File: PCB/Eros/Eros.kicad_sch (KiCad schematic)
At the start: 89 parts, among them J1 USB_C_PowerOnly_6P, J2 UART, J3 Li-ion, J4 Conn_01x08_Socket, J6 Micro_SD_Card, Q1 BC817, SW1 SW_Push, SW2 SW_Push, SW3 SW_Push, SW4 SW_Push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

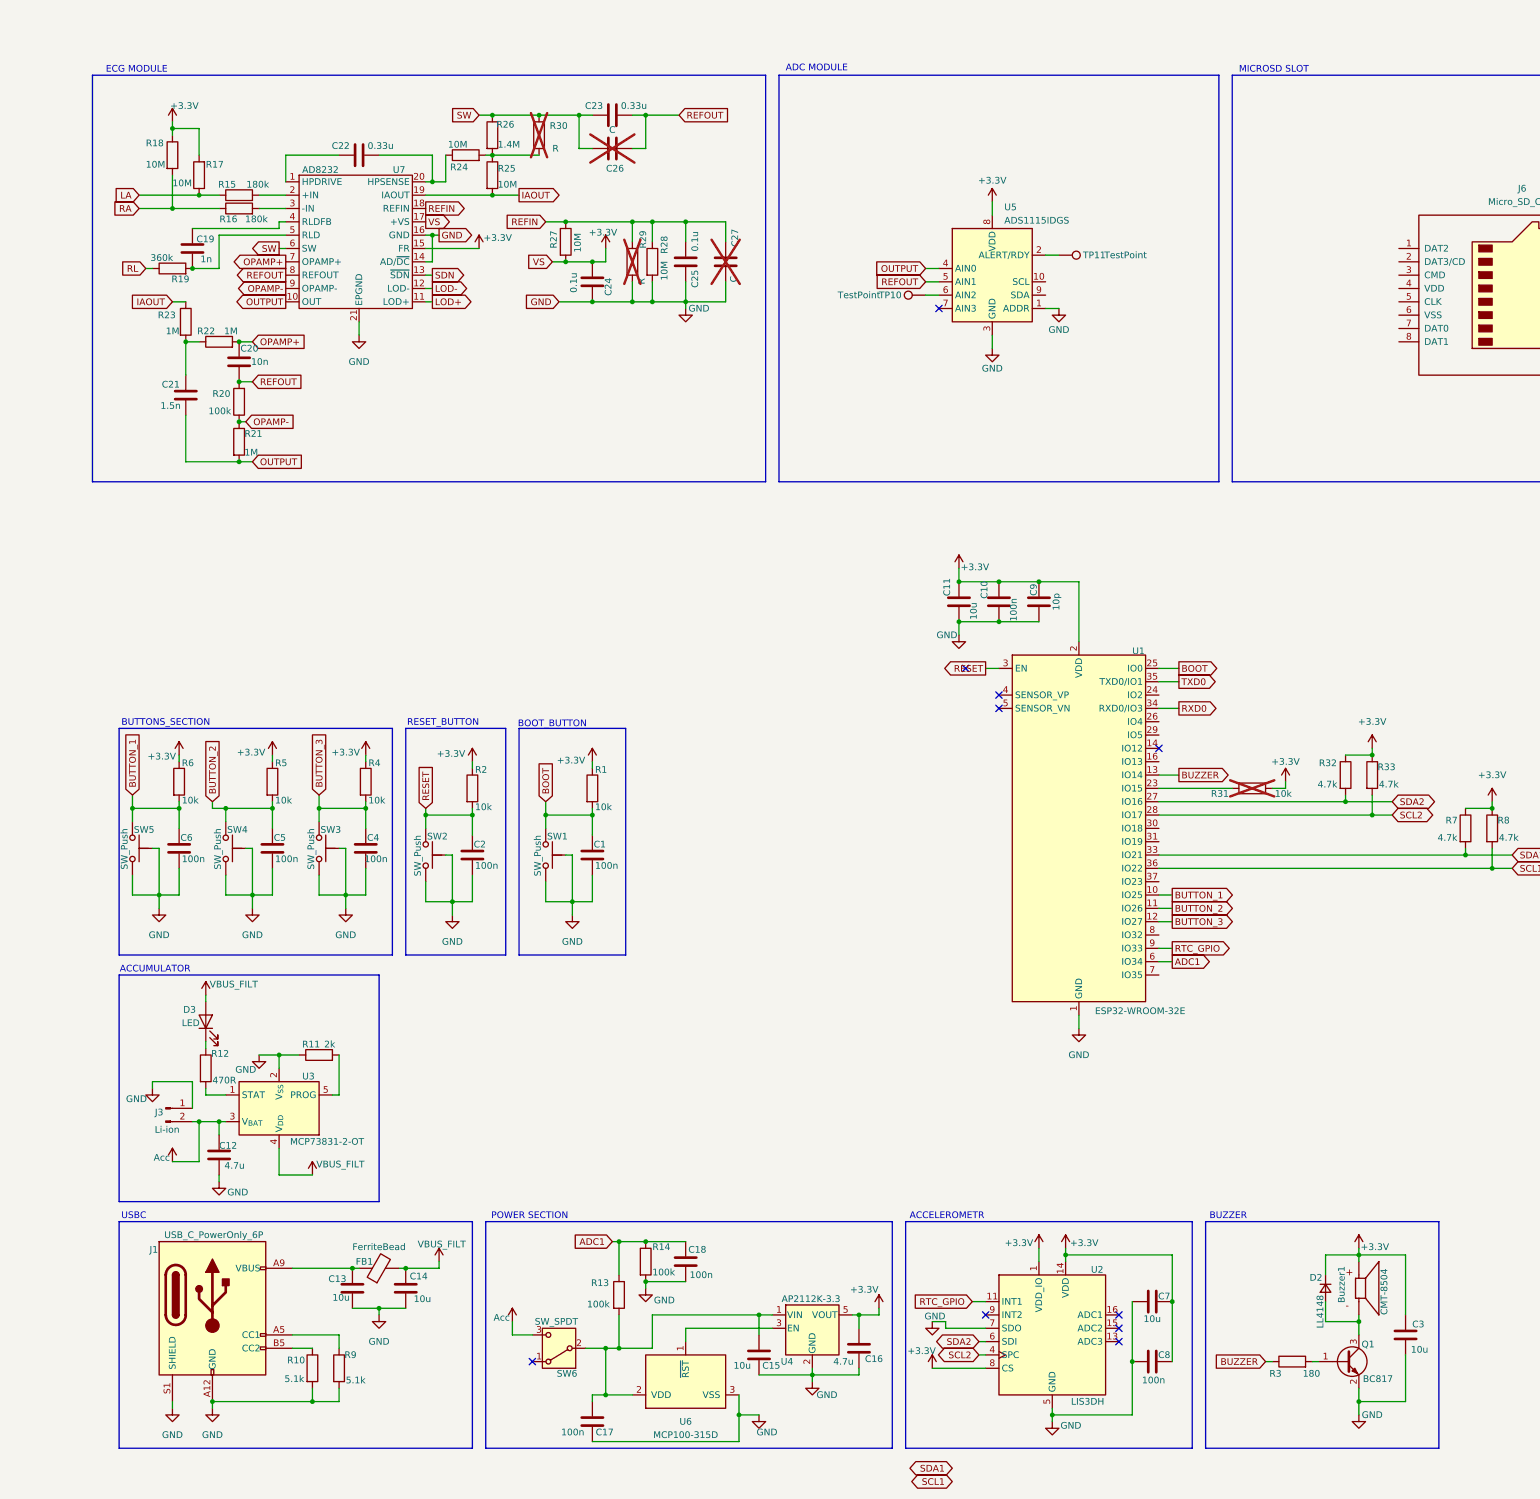
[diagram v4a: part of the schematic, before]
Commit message: Wire SDcard SPI
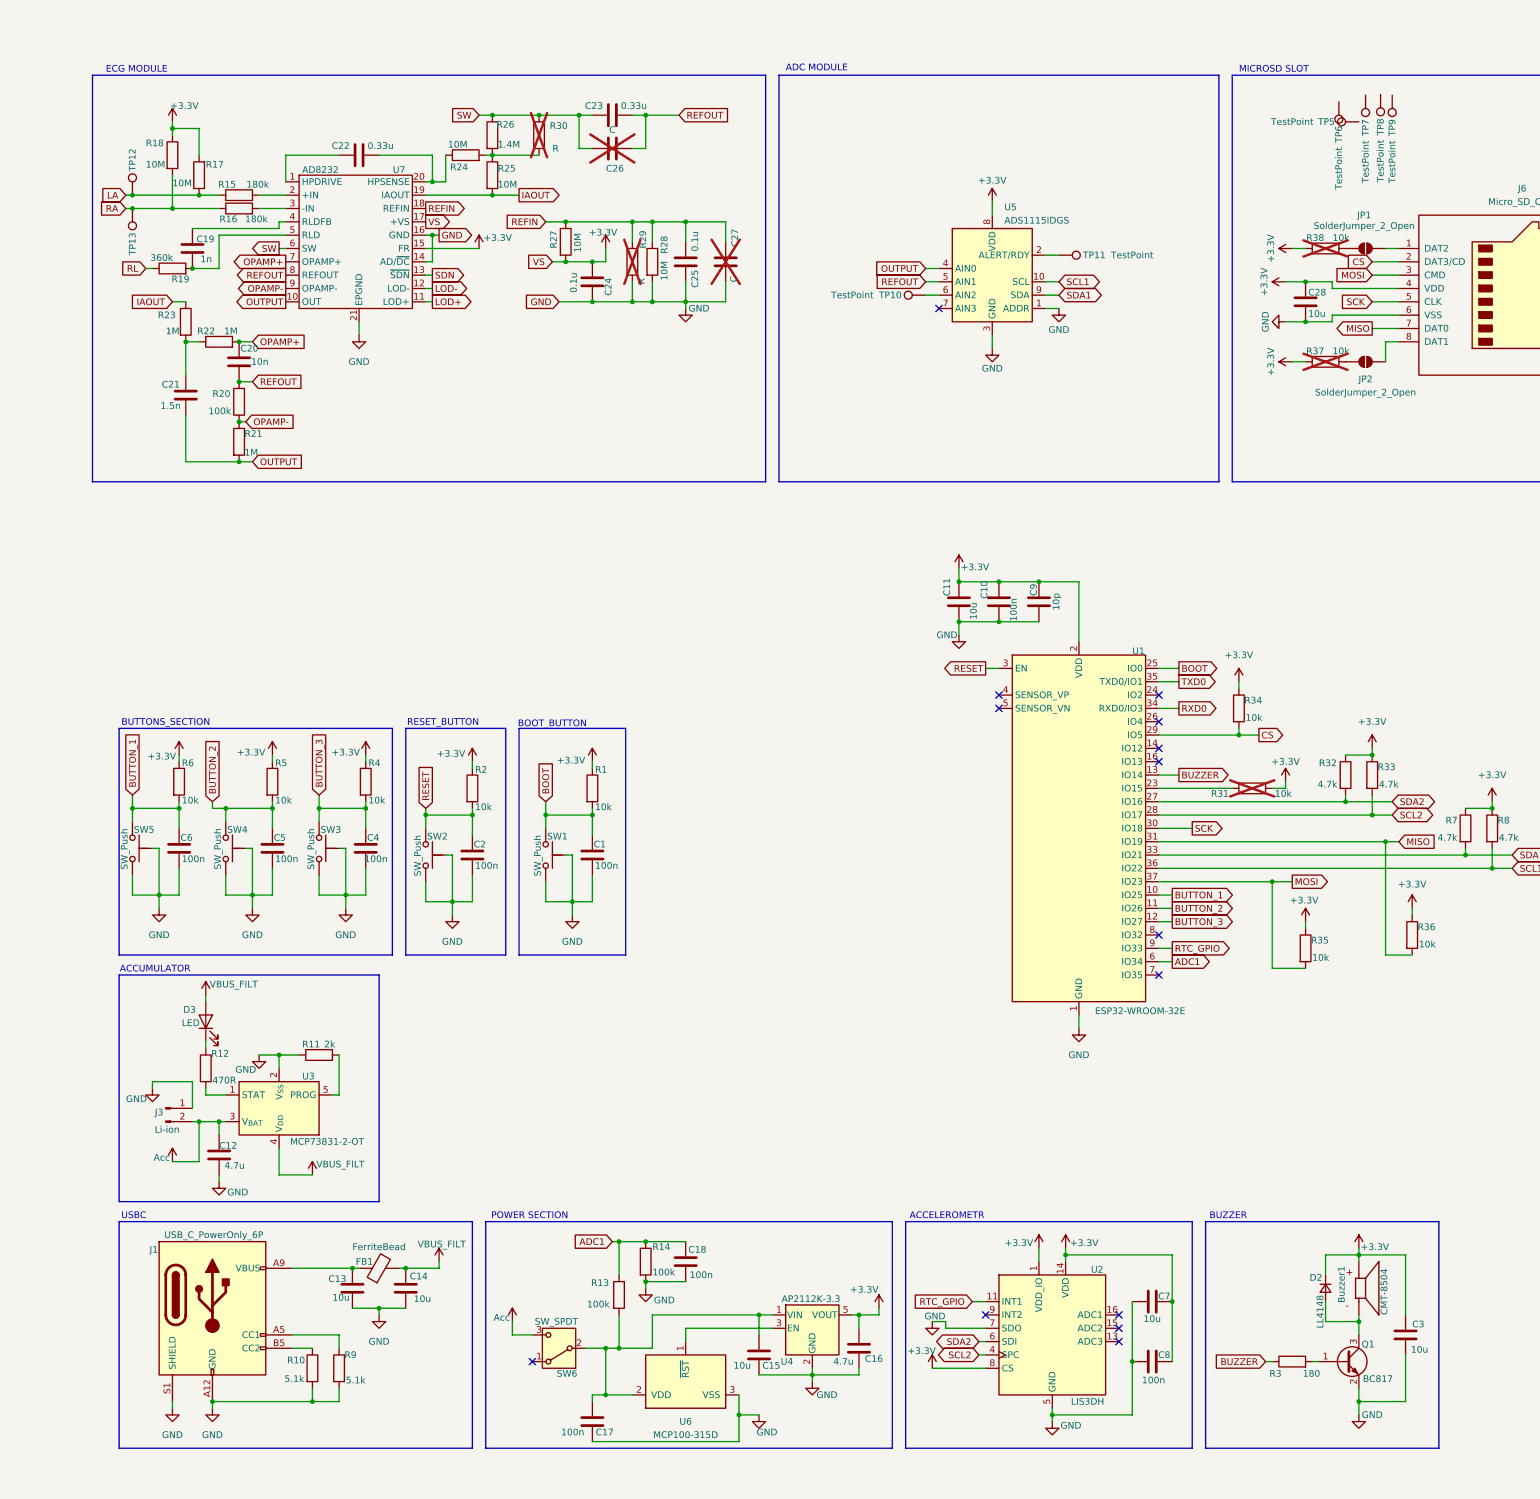
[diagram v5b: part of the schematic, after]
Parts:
- added C28: 10u, Capacitor_SMD:C_0402_1005Metric, symbol Device:C
- added JP1, JP2: SolderJumper_2_Open, symbol Jumper:SolderJumper_2_Open
- added R34, R35, R36, R37, R38: 10k, Resistor_SMD:R_0402_1005Metric, symbol Device:R
- added TP12, TP13, TP5, TP6, TP7, TP8, TP9: TestPoint, TestPoint:TestPoint_Pad_D1.5mm, symbol Connector:TestPoint
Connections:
- net +3.3V: now also J6.4 (VDD), C28.1, R34.1, R35.1, R36.1, R37.1, R38.1
- net GND: now also J6.6 (VSS), C28.2
- net LA: now also TP12.1
- net RA: now also TP13.1
- net SCL1: now also U5.10 (SCL)
- net SDA1: now also U5.9 (SDA)
- net at J6.1 (DAT2): now also JP1.2 (B)
- net CS: now reaches J6.2 (DAT3/CD)
- net CS: now also U1.29 (IO5), R34.2
- net MOSI: now reaches J6.3 (CMD)
- net MOSI: now also U1.37 (IO23), R35.2
- net SCK: now reaches J6.5 (CLK)
- net SCK: now also U1.30 (IO18)
- net MISO: now reaches J6.7 (DAT0)
- net MISO: now also U1.31 (IO19), R36.2
- net at J6.8 (DAT1): now also JP2.2 (B)
- new net: JP1.1 (A), R38.2
- new net: JP2.1 (A), R37.2
- no-connect marks 10 -> 14

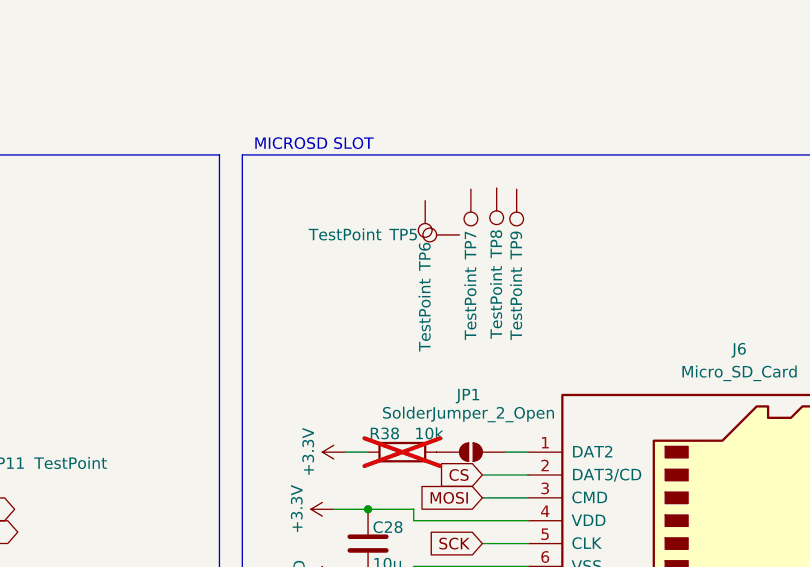
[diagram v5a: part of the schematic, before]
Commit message: add footprints and tps
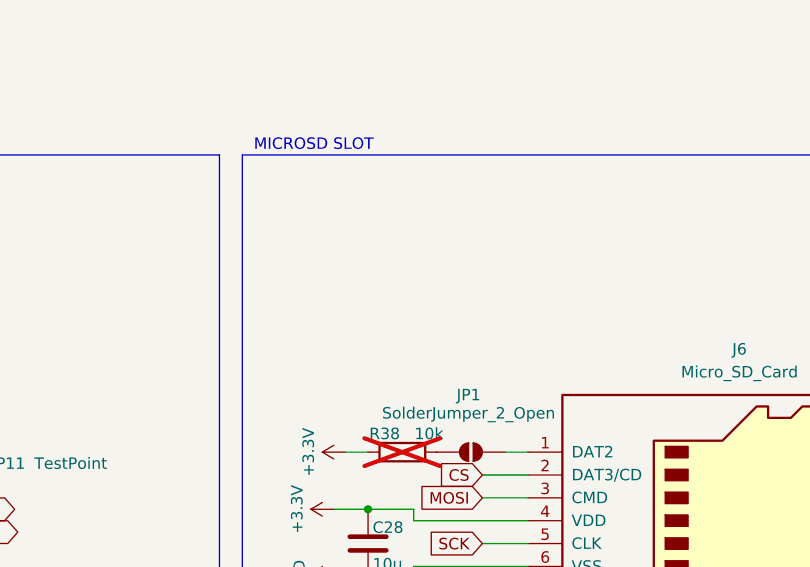
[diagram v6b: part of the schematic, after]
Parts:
- removed TP5, TP6, TP7, TP8, TP9: TestPoint, TestPoint:TestPoint_Pad_D1.5mm, symbol Connector:TestPoint
- C1, C10, C17, C18, C2, C28, C4, C5, C6, C8, C9, R13, R14: footprint Capacitor_SMD:C_0402_1005Metric -> Capacitor_SMD:C_0402_1005Metric_Pad0.74x0.62mm_HandSolder
- C11, C12, C13, C14, C15, C16, C3, C7: footprint Capacitor_SMD:C_0603_1608Metric -> Capacitor_SMD:C_0603_1608Metric_Pad1.08x0.95mm_HandSolder
- C19, C20, C21, C22, C23, C24, C25: footprint (none) -> Capacitor_SMD:C_0402_1005Metric_Pad0.74x0.62mm_HandSolder
- D3: footprint LED_SMD:LED_0402_1005Metric -> LED_SMD:LED_0402_1005Metric_Pad0.77x0.64mm_HandSolder
- FB1: footprint Inductor_SMD:L_0402_1005Metric -> Inductor_SMD:L_0402_1005Metric_Pad0.77x0.64mm_HandSolder
- J4: footprint (none) -> LED_SMD:LED_0402_1005Metric_Pad0.77x0.64mm_HandSolder
- JP1, JP2: footprint (none) -> Jumper:SolderJumper-2_P1.3mm_Open_Pad1.0x1.5mm
- R1, R10, R11, R12, R2, R3, R32, R33, R35, R36, R37, R38, R4, R5, R6, R7, R8, R9: footprint Resistor_SMD:R_0402_1005Metric -> Resistor_SMD:R_0402_1005Metric_Pad0.72x0.64mm_HandSolder
- R15, R16, R17, R18, R19, R20, R21, R22, R23, R24, R25, R26, R27, R28: footprint (none) -> Resistor_SMD:R_0402_1005Metric_Pad0.72x0.64mm_HandSolder
- R34: footprint Resistor_SMD:R_0402_1005Metric -> Resistor_SMD:R_01005_0402Metric_Pad0.57x0.30mm_HandSolder

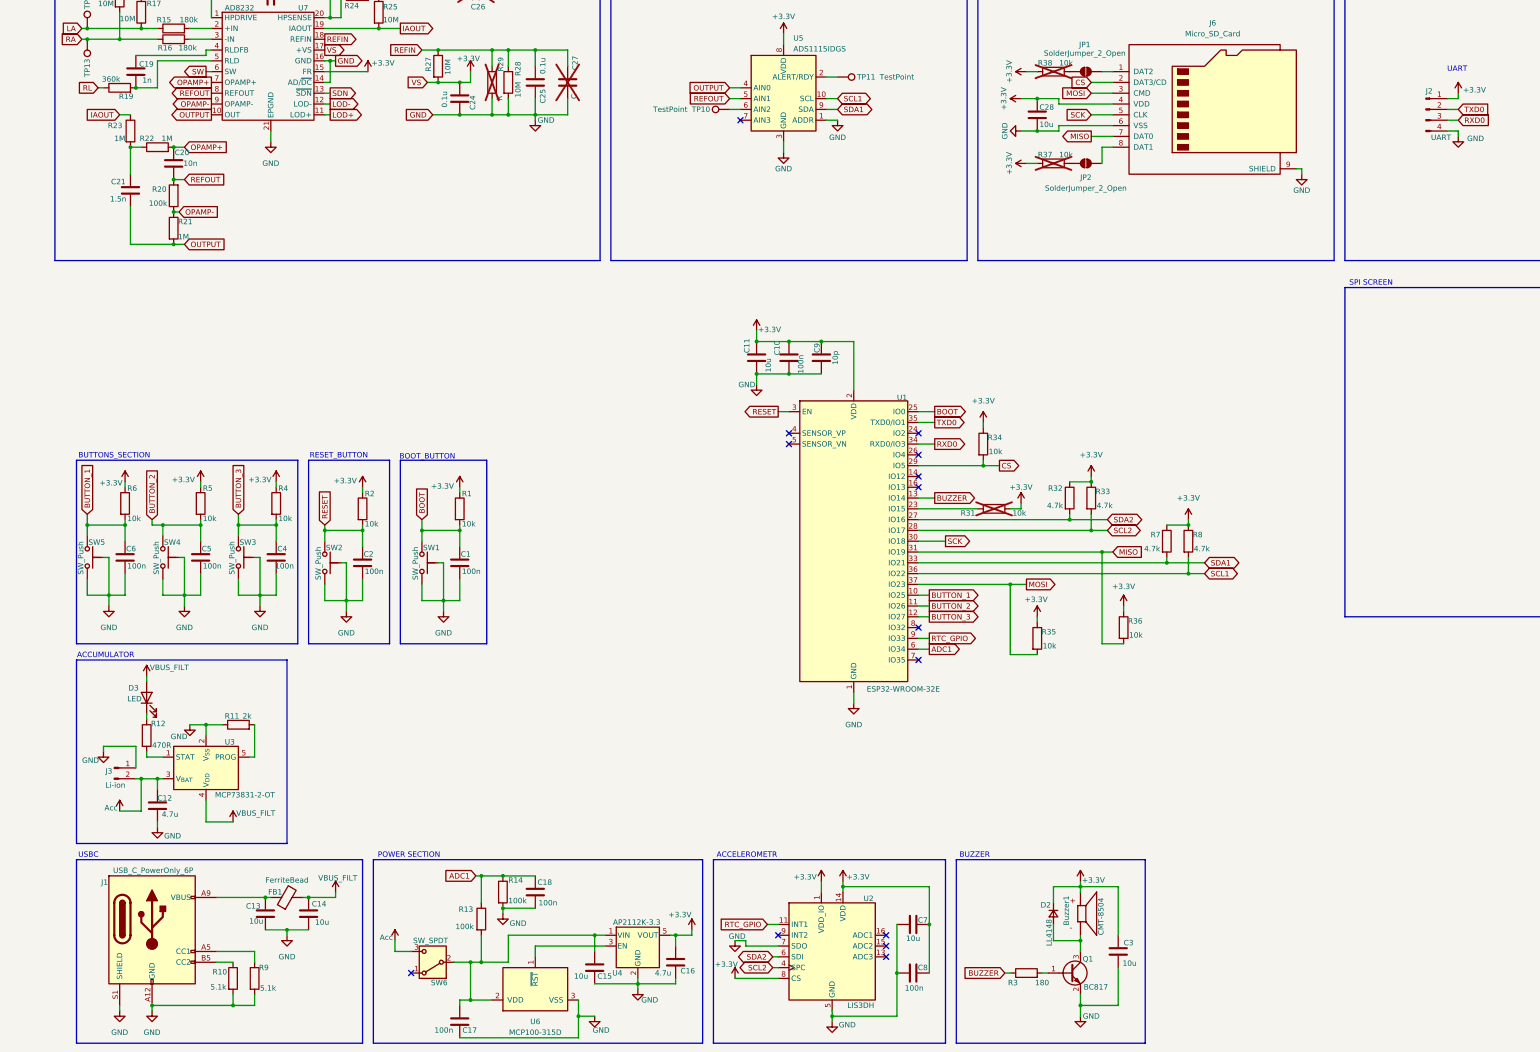
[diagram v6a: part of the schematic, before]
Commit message: add VSPI and HSPI flags
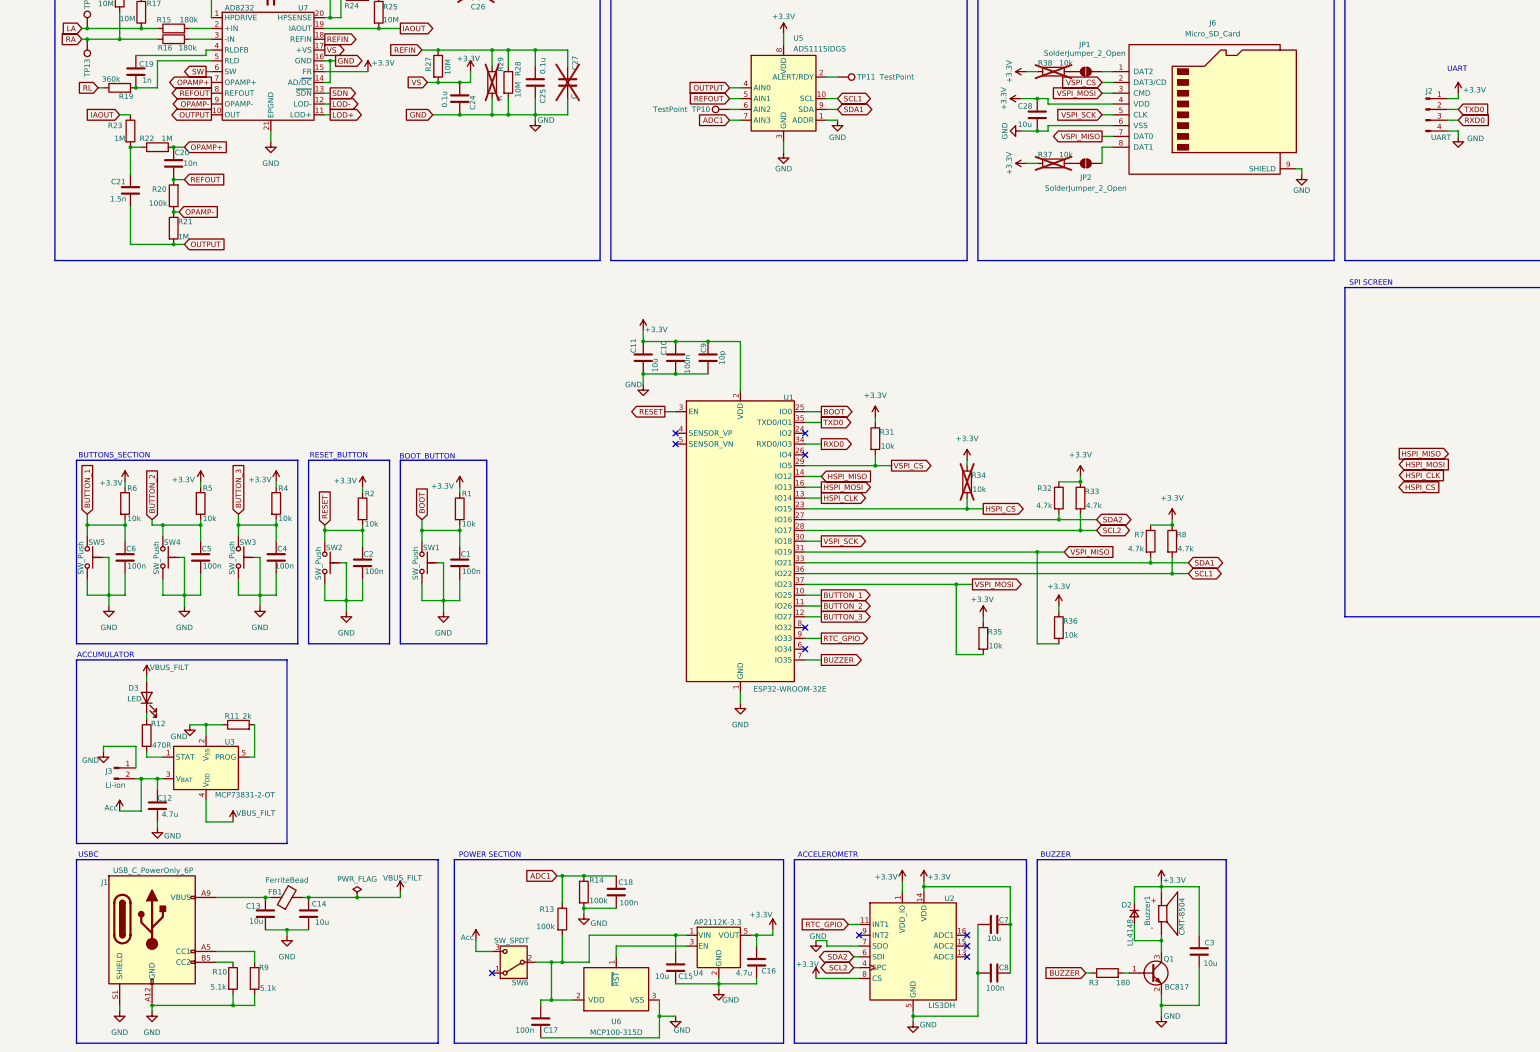
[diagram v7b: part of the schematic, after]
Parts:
- R31: footprint Resistor_SMD:R_0402_1005Metric_Pad0.72x0.64mm_HandSolder -> Resistor_SMD:R_01005_0402Metric_Pad0.57x0.30mm_HandSolder; now fitted
- R34: now not fitted
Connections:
- net ADC1: now also U5.7 (AIN3); no longer U1.6 (IO34)
- net BUZZER: now also U1.7 (IO35); no longer U1.13 (IO14)
- net HSPI_CS: now reaches U1.23 (IO15)
- net HSPI_CS: now also R34.2; no longer R31.2
- net HSPI_MISO: now reaches U1.14 (IO12)
- net HSPI_MOSI: now reaches U1.16 (IO13)
- net CS renamed VSPI_CS
- net VSPI_CS: now also R31.2; no longer R34.2
- net MISO renamed VSPI_MISO
- net MOSI renamed VSPI_MOSI
- net SCK renamed VSPI_SCK
- new net HSPI_CLK: U1.13 (IO14)
- no-connect marks 14 -> 11
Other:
- moved on the sheet: Buzzer1, C10, C11, C15, C16, C17, C18, C3, C7, C8, C9, D2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
